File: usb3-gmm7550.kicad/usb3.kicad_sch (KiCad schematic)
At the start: 18 parts, among them U1 ECMF02-2AMX6, U3 LM66200DRLR

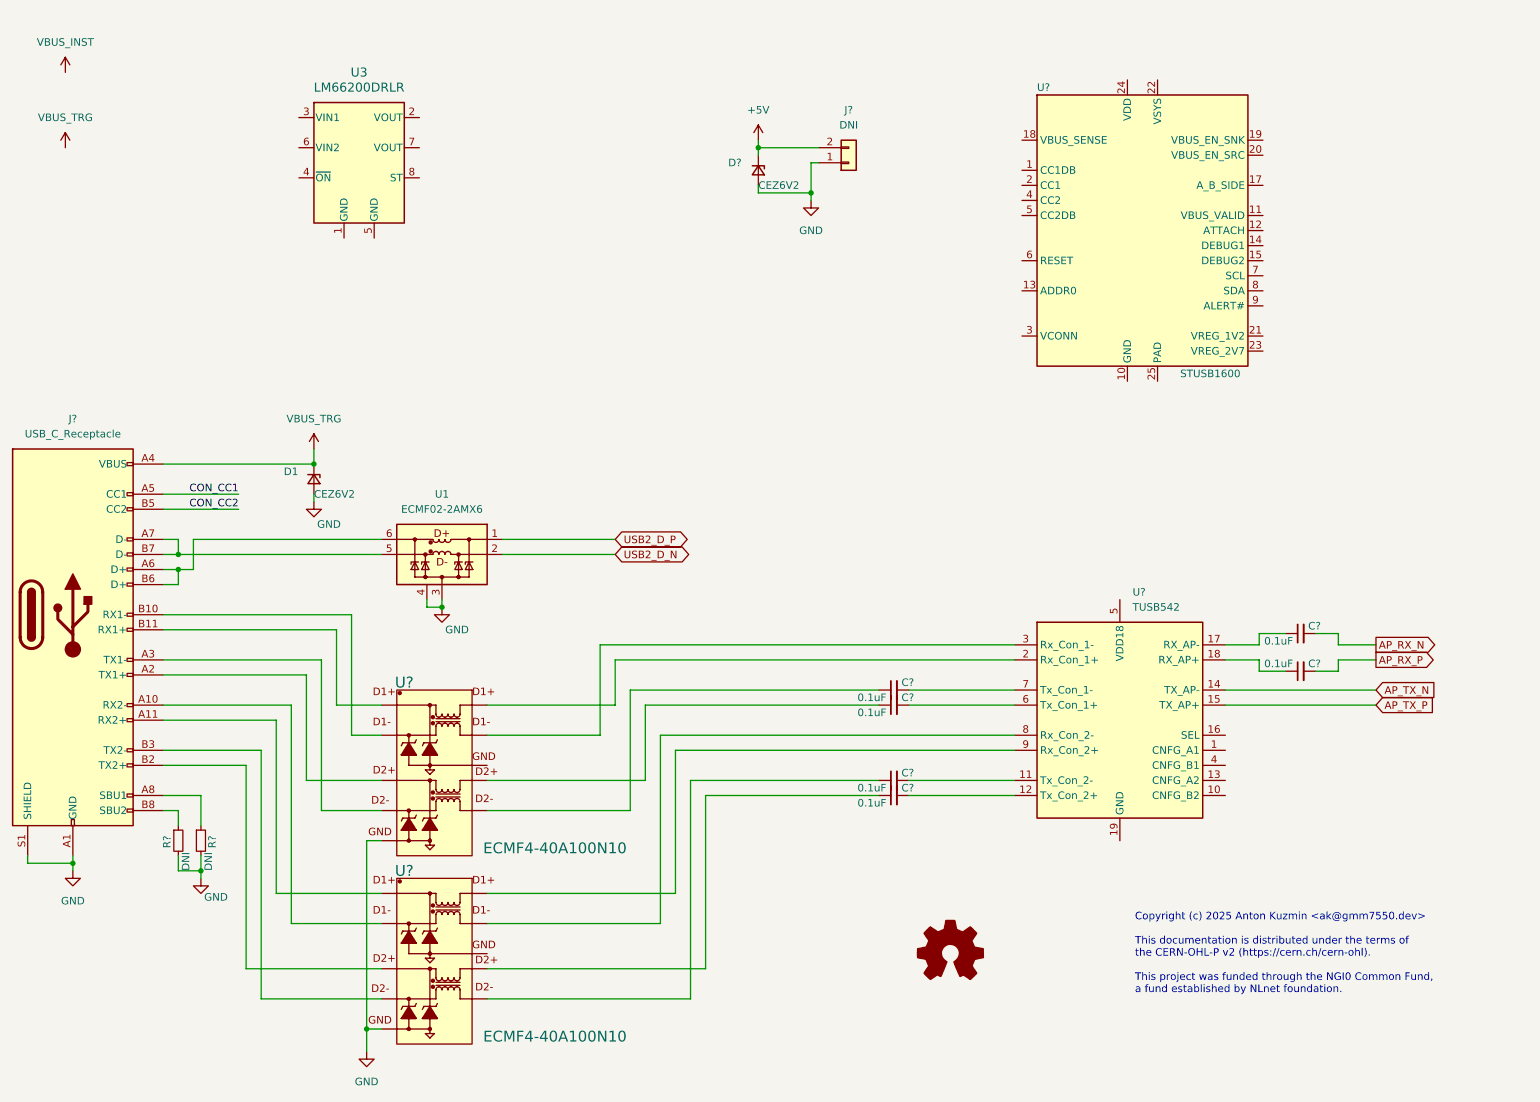
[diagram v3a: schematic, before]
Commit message: USB 3 adapter schematic -- WIP: USB 3 and Power Delivery pages
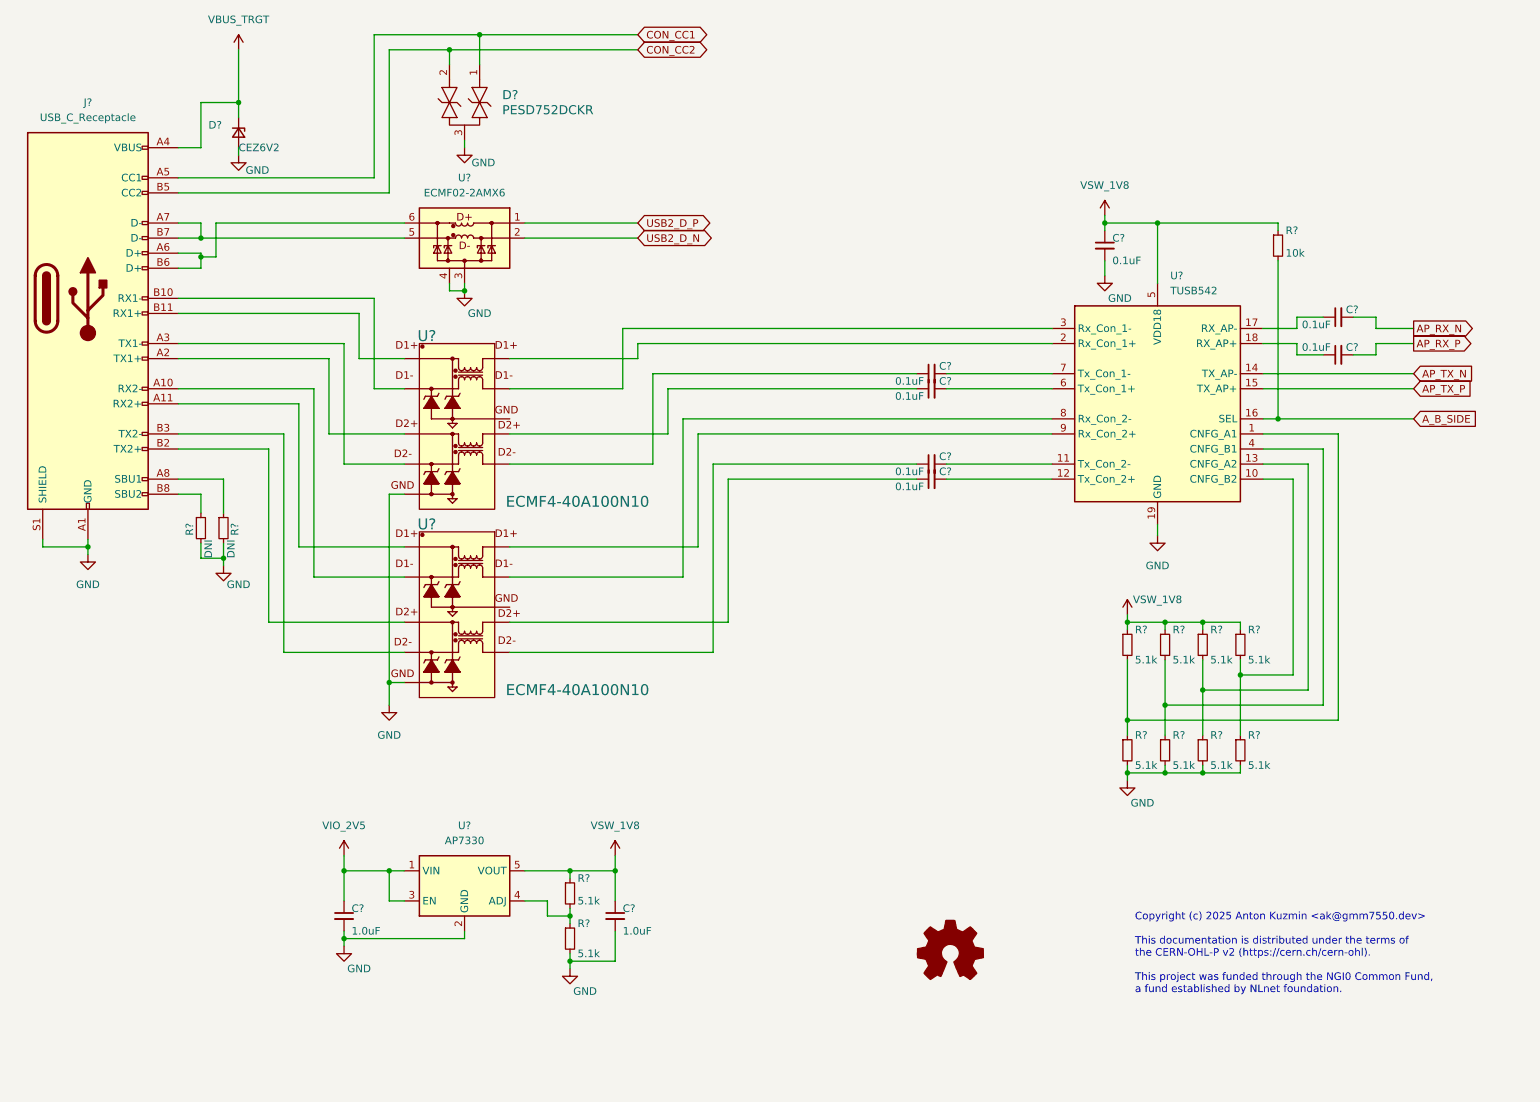
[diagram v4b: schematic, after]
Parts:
- removed D?: CEZ6V2, Diode_SMD:D_SOD-523, symbol Device:D_Zener_Small
- removed J?: DNI, Connector_Molex:Molex_Micro-Fit_3.0_43045-0200_2x01_P3.00mm_Horizontal, symbol Connector_Generic:Conn_01x02
- removed U3: LM66200DRLR, SOT-5X3_DRL_TEX, symbol usb3-gmm7550:LM66200DRLR
- removed U?: STUSB1600, Package_DFN_QFN:QFN-24-1EP_4x4mm_P0.5mm_EP2.7x2.7mm_ThermalVias, symbol usb3-gmm7550:STUSB1600
- added C?: 0.1uF, Capacitor_SMD:C_0402_1005Metric, symbol Device:C_Small
- added C? (x2): 1.0uF, Capacitor_SMD:C_0402_1005Metric, symbol Device:C_Small
- added D?: PESD752DCKR, SOT-SC70_DCK_TEX, symbol usb3-gmm7550:PESD752DCKR
- added R? (x10): 5.1k, Resistor_SMD:R_0402_1005Metric, symbol Device:R_Small
- added R?: 10k, Resistor_SMD:R_0402_1005Metric, symbol Device:R_Small
- added U?: AP7330, Package_TO_SOT_SMD:SOT-23-5, symbol usb3-gmm7550:AP7330
- renumbered D1 to D?, U1 to U?
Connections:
- net CON_CC1: now also D?.1
- net CON_CC2: now also D?.2
- net GND: now also U?.19 (GND), C?.2, C?.2, C?.2, D?.3, R?.2, R?.2, R?.2, R?.2, R?.2, U?.2 (GND)
- net at U?.1 (CNFG_A1): now also R?.1, R?.2
- net at U?.10 (CNFG_B2): now also R?.1, R?.2
- net at U?.13 (CNFG_A2): now also R?.1, R?.2
- net A_B_SIDE: now reaches U?.16 (SEL)
- net A_B_SIDE: now also R?.2
- net at U?.4 (CNFG_B1): now also R?.1, R?.2
- net VSW_1V8: now reaches U?.5 (VDD18)
- net VSW_1V8: now also C?.1, C?.1, R?.1, R?.1, R?.1, R?.1, R?.1, R?.1, U?.5 (VOUT)
- net VBUS_TRG renamed VBUS_TRGT
- new net: R?.1, R?.2, U?.4 (ADJ)
- new net VIO_2V5: C?.1, U?.1 (VIN), U?.3 (EN)
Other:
- moved on the sheet: C?, D?, J?, R?, U?

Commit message: USB 3 adapter schematic -- WIP: USB 1.1 and 2.0 page, connections to the GMM-7550 IOs
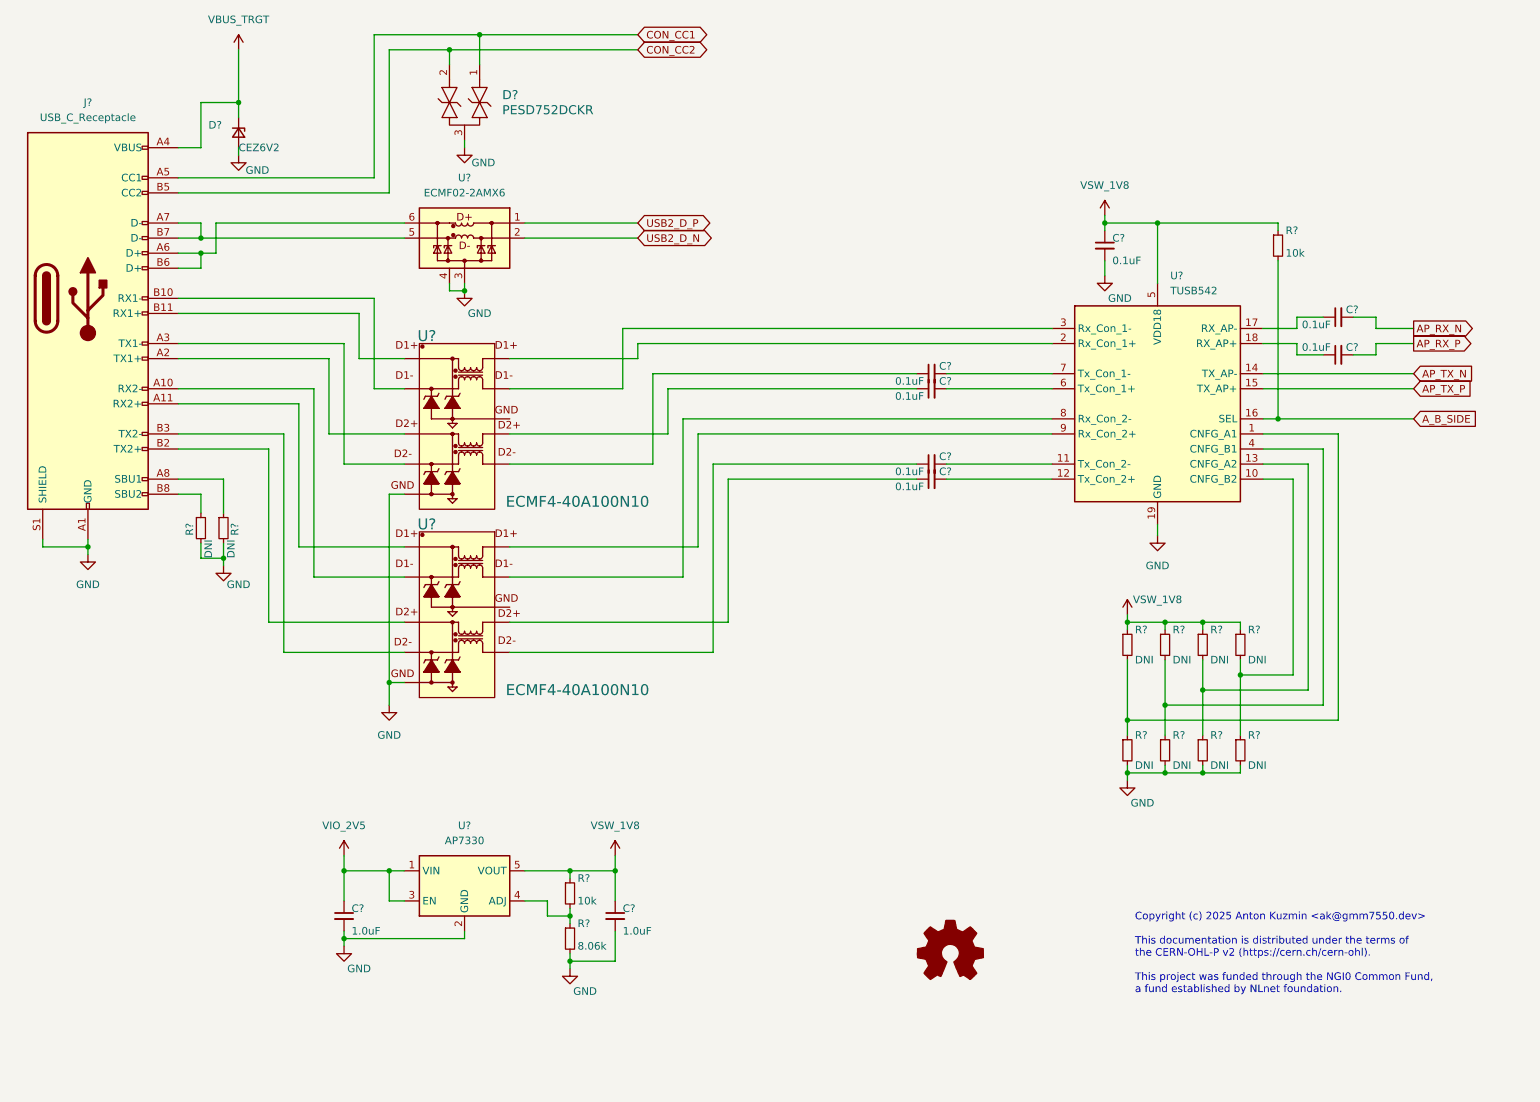
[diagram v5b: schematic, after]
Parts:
- R? (x8): value 5.1k -> DNI
- R?: value 5.1k -> 10k
- R?: value 5.1k -> 8.06k
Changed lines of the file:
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@@
 	)
 	(junction
-		(at 57.15 56.515)
-		(diameter 0)
-		(color 0 0 0 0)
-	)
-	(junction
 		(at 226.06 118.11)
 		(diameter 0)
@@
 	)
 	(junction
+		(at 57.15 55.88)
+		(diameter 0)
+		(color 0 0 0 0)
+	)
+	(junction
 		(at 219.71 143.51)
 		(diameter 0)
@@
 	(wire
 		(pts
-			(xy 57.15 58.42) (xy 57.15 56.515)
-		)
-		(stroke
-			(width 0)
-			(type default)
-		)
-	)
-	(wire
-		(pts
 			(xy 251.46 66.675) (xy 255.27 66.675)
 		)
@@
 	(wire
 		(pts
-			(xy 59.69 56.515) (xy 57.15 56.515)
+			(xy 59.69 55.88) (xy 57.15 55.88)
 		)
 		(stroke
@@
 	(wire
 		(pts
-			(xy 59.69 50.8) (xy 59.69 56.515)
+			(xy 59.69 50.8) (xy 59.69 55.88)
 		)
 		(stroke
@@
 	(wire
 		(pts
-			(xy 57.15 55.88) (xy 57.15 56.515)
+			(xy 57.15 55.88) (xy 57.15 58.42)
 		)
 		(stroke
@@
 			"AAAAAABwrVimNl8AAAAAAAAAAAAAAAAAAAAAAAAhAAAAAAAAAHAcblUzXwAAYOptVTNfAABgAQAA"
 			"AAAAAFAAAAAAAAAA8FlbpjZfAAAAAAAAAAAAAAAAAAAAAAAAoNIE85Z8AAAAAACAAAAAAAAAAAAA"
-			"AAAAAAAAAAAAAAAAAA=="
+			"AAAAAAAAAAAAAAAAAAAAZwAAADMAAAB6AAAAZAAAADYAAAAyAAAAeQAAAEQAAABCAAAAeQAAAGMA"
+			"AABIAAAAMgAAAE8AAABKAAAAYgAAAEEAAABPAAAAVgAAAEoAAAAzAAAAVwAAADEAAAB2AAAAdAAA"
+			"AEEAAABaAAAAWgAAAHAAAABnAAAANQAAAGkAAABkAAAAMAAAAHgAAABOAAAAMAAAAEMAAABqAAAA"
+			"SgAAAEsAAAAxAAAATQAAAEUAAABwAAAATwAAAG4AAABNAAAASQAAAFMAAABBAAAAVwAAAGMAAABD"
+			"AAAAegAAAHcAAABMAAAAMAAAADkAAABNAAAAZQAAAEwAAABMAAAAZAAAAC8AAABPAAAAdwAAAE4A"
+			"AAB0AAAAZQAAAE0AAABEAAAARQAAAEYAAABuAAAAMQAAAFcAAAB0AAAAYwAAAEYAAAB4AAAAUQAA"
+			"ADQAAABzAAAAUQAAAFUAAAA5AAAAVAAAACsAAABhAAAAegAAAGgAAAAyAAAAVwAAAFoAAABFAAAA"
+			"QgAAAEQAAABFAAAAcwAAAEQAAABMAAAAbAAAAGEAAABQAAAAWQAAAFQAAABHAAAARAAAAE0AAABs"
+			"AAAAdwAAAGoAAAB4AAAAbgAAAFMAAABPAAAATQAAAGIAAABFAAAAaAAAAGgAAABmAAAASwAAAE4A"
+			"AAB3AAAAVgAAAEsAAABUAAAAdAAAAEQAAAByAAAAdwAAAFMAAAB3AAAATAAAAFcAAABuAAAAOAAA"
+			"AEYAAAB2AAAAcwAAAHAAAABJAAAAQwAAAEkAAAB3AAAAcAAAAGoAAABBAAAAQQAAAFMAAABrAAAA"
+			"SQAAADkAAABlAAAAdgAAAC8AAABQAAAAdgAAAEoAAABZAAAAYQAAADMAAAB6AAAATgAAADAAAAB6"
+			"AAAAagAAAE0AAAB4AAAAbgAAAFIAAABBAAAASQAAADEAAABJAAAAWgAAAFUAAABTAAAATQAAADgA"
+			"AABvAAAAbQAAAEkAAABBAAAAbwAAAGUAAAB1AAAATwAAADcAAABUAAAAdQAAAFgAAABTAAAAVAAA"
+			"AGUAAAA4AAAARwAAAGUAAABzAAAAKwAAAHcAAABEAAAARwAAAE8AAABDAAAAZAAAAFYAAABJAAAA"
+			"UwAAAHAAAABxAAAAMAAAAHUAAAA2AAAAbwAAAHIAAABLAAAAcwAAAG4AAABoAAAAVQAAAGoAAABq"
+			"AAAAeAAAAEQAAABvAAAANQAAADgAAABVAAAAYgAAAGkAAAAvAAAATQAAAFUAAABPAAAAYQAAAHEA"
+			"AAA2AAAAcwAAAEsAAABTAAAALwAAAFgAAAB0AAAANAAAAEMAAABCAAAAYQAAADkAAAB4AAAAVQAA"
+			"AHUAAAAzAAAAcAAAAA=="
 		)
 	)
@@
 			"UjNfAAAAAAAAKQAAACkAAAAAAAAAWFs0UjNfAADjAwAASgAAAOMDAABLAAAAAAAAAHIAAADgYTRS"
 			"M18AAJhiNFIzXwAAaGI0UjNfAABoYjRSM18AAGhiNFIzXwAAACEwUhQBAACwITBSM18AANAhMFIz"
-			"XwAAXAIAAA4AAABcAgAAEw=="
+			"XwAAXAIAAA4AAABcAgAAE0FBQUFBQUFBQUFBQUFBQUFBQUFBQUFBQUFBQUFBQUFBQUFBQUFBQUFB"
+			"QUFBQUFBQUFBQUFBQUFBQUFBQUFBQUFBQUFBQUFBQUFBQUFBQUFBQUFBQUFBQUFBQUFBQUFBQUFB"
+			"QUFBQUFBQUFBQUFBQUFBQUFBQUFBQUFBQUFBQUFBQUFBQUFBQUFBQUFBQUFBQUFBQUFBQUFBQUFB"
+			"QUFBQUFBQUFBQUFBQUFBQUFBQUFBQUFBQUFBQUFBQUFBQUFBQUFBQUFBQUFBQUFBQUFBQUFBQUFB"
+			"QUFBQUFBQUFBQUFBQUFBQUFBQUFBQUFBQUFBQUFBQUFBQUFBQUFBQUFBQUFBQUFBQUFBQUFBQUFB"
+			"QUFBQUFBQUFBQUFBQUFBQUFBQUFBQUFBQUFBQUFBQUFBQUFBQUFBQUFBQUFBQUFBQUFBQUFBQUFB"
+			"QUFBQUFBQUFBQUFBQUFBQUFBQUFBQUFBQUFBQUFBQUFBQUFBQUFBQUFBQUFBQUFBQUFBQUFBQUFB"
+			"QUFBQUFBQUFBQUFBQUFBQUFBQUFBQUFBQUFBQUFBQUFBQUFBQUFBQUFBQUFBQUFBQUFBQUFBQUFB"
+			"QUFBQUFBQUFBQUFBQUFBQUFBQUFBQUFBQUFBQUFBQUFBQUFBQUFBQUFBQUFBQUFBQUFBQUFBQUFB"
+			"QUFBQUFBQUFBQUFBQUFBQUFBQUFBQUFBQUFBQUFBQUFBQUFBQUFBQUFBQUFBQUFBQUFBQUFBQUFB"
+			"QUFBQUFBQUFBQUFBQUFBQUFBQUFBQUFBQUFBQUFBQUFBQUFBQUFBQUFBQUFBQUFBQUFBQUFBQUFB"
+			"QUFBQUFBQUFBQUFBQUFBQUFBQUFBQUFBQUFBQUFBQUFBQUFBQUFBQUFBQUFBQUFBQUFBQUFFQUxi"
+			"bFV6WHdBQXdFWGk4Slo4QUFDQkFBQUFBQUFBQUFBS2JsVXpYd0FBSU92UDc1WjhBQUJRQ201Vk0x"
+			"OEFBS0FEQnZPV2ZBQUFPUUFBQUFBQUFBQmdEWEZWTTE4QUFGRG1CUE9XZkFBQVFRQUFBQUFBQUFB"
+			"ZzVtMVZNMThBQUpDTndWSXpYd0FBQUFBQUFBQUFBQUFBQUFBQTdBQUFBQUFBQUFBQkFBSUFVQWh1"
+			"VlROZkFBREFBUUFBQUFBQUFGQUFBQUFBQUFBQVVGOWJwalpmQUFBd3d3WHpsbndBQVBBRmJsVXpY"
+			"d0FBTU80Rjg1WjhBQUNBQjI1Vk0xOEFBTUNBQnZPV2ZBQUFnQWR1VlROZkFBREFnQWJ6bG53QUFB"
+			"QUFBQUFBQUFBQU1RQUFBQUFBQUFDZ24yNVZNMThBQU5ENGJWVXpYd0FBMEtETThKWjhBQUR3Qlc1"
+			"Vk0xOEFBRUFDQUFBQUFBQQ=="
 		)
 	)
@@
 		(on_board yes)
 		(dnp no)
-		(property "Reference" "#PWR06"
+		(property "Reference" "#PWR?"
 			(at 63.5 45.72 0)
 			(effects
@@
 			(project "usb3-gmm7550"
 				(path "/e63e39d7-6ac0-4ffd-8aa3-1841a4541b55/201c9a67-de5c-41f6-bf23-7bce60956be5"
-					(reference "#PWR06")
+					(reference "#PWR?")
 					(unit 1)
 				)
@@
 			)
 		)
-		(property "Value" "5.1k"
+		(property "Value" "DNI"
 			(at 220.98 142.24 0)
 			(effects
@@
 		(on_board yes)
 		(dnp no)
-		(property "Reference" "#PWR02"
+		(property "Reference" "#PWR?"
 			(at 213.36 120.65 0)
 			(effects
@@
 			(project "usb3-gmm7550"
 				(path "/e63e39d7-6ac0-4ffd-8aa3-1841a4541b55/201c9a67-de5c-41f6-bf23-7bce60956be5"
-					(reference "#PWR02")
+					(reference "#PWR?")
 					(unit 1)
 				)
@@
 			)
 		)
-		(property "Value" "5.1k"
+		(property "Value" "10k"
 			(at 120.65 165.1 0)
 			(effects
@@
 			)
 		)
-		(property "Value" "5.1k"
+		(property "Value" "DNI"
 			(at 214.63 142.24 0)
 			(effects
@@
 			)
 		)
-		(property "Value" "5.1k"
-			(at 120.65 173.99 0)
+		(property "Value" "8.06k"
+			(at 120.65 172.72 0)
 			(effects
 				(font
@@
 			)
 		)
-		(property "Value" "5.1k"
+		(property "Value" "DNI"
 			(at 233.68 142.24 0)
 			(effects
@@
 			)
 		)
-		(property "Value" "5.1k"
+		(property "Value" "DNI"
 			(at 233.68 124.46 0)
 			(effects
@@
 		(on_board yes)
 		(dnp no)
-		(property "Reference" "#PWR04"
+		(property "Reference" "#PWR?"
 			(at 81.28 179.07 0)
 			(effects
@@
 			(project "usb3-gmm7550"
 				(path "/e63e39d7-6ac0-4ffd-8aa3-1841a4541b55/201c9a67-de5c-41f6-bf23-7bce60956be5"
-					(reference "#PWR04")
+					(reference "#PWR?")
 					(unit 1)
 				)
@@
 			)
 		)
-		(property "Value" "5.1k"
+		(property "Value" "DNI"
 			(at 227.33 124.46 0)
 			(effects
@@
 		(on_board yes)
 		(dnp no)
-		(property "Reference" "#PWR01"
+		(property "Reference" "#PWR?"
 			(at 213.36 151.13 0)
 			(effects
@@
 			(project ""
 				(path "/e63e39d7-6ac0-4ffd-8aa3-1841a4541b55/201c9a67-de5c-41f6-bf23-7bce60956be5"
-					(reference "#PWR01")
+					(reference "#PWR?")
 					(unit 1)
 				)
@@
 			)
 		)
-		(property "Value" "5.1k"
+		(property "Value" "DNI"
 			(at 227.33 142.24 0)
 			(effects
@@
 		(on_board yes)
 		(dnp no)
-		(property "Reference" "#PWR03"
+		(property "Reference" "#PWR?"
 			(at 209.55 66.04 0)
 			(effects
@@
 			(project "usb3-gmm7550"
 				(path "/e63e39d7-6ac0-4ffd-8aa3-1841a4541b55/201c9a67-de5c-41f6-bf23-7bce60956be5"
-					(reference "#PWR03")
+					(reference "#PWR?")
 					(unit 1)
 				)
@@
 			)
 		)
-		(property "Value" "5.1k"
+		(property "Value" "DNI"
 			(at 220.98 124.46 0)
 			(effects
@@
 		(on_board yes)
 		(dnp no)
-		(property "Reference" "#PWR05"
+		(property "Reference" "#PWR?"
 			(at 119.38 182.88 0)
 			(effects
@@
 			(project "usb3-gmm7550"
 				(path "/e63e39d7-6ac0-4ffd-8aa3-1841a4541b55/201c9a67-de5c-41f6-bf23-7bce60956be5"
-					(reference "#PWR05")
+					(reference "#PWR?")
 					(unit 1)
 				)
@@
 			)
 		)
-		(property "Value" "5.1k"
+		(property "Value" "DNI"
 			(at 214.63 124.46 0)
 			(effects
